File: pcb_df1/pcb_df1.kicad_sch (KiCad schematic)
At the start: 6 parts, among them J1 Cable, J2 Floppy, Q1 DMG2301L, Q2 BSS123

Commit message: DF1 (floppy detection) PCB completed.
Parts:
- J1, J2: footprint (none) -> pcb_df1:idc34_edge
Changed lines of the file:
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@@
       (effects (font (size 1.27 1.27)))
     )
-    (property "Footprint" "" (at 34.925 50.165 0)
+    (property "Footprint" "pcb_df1:idc34_edge" (at 34.925 50.165 0)
       (effects (font (size 1.27 1.27)) hide)
     )
@@
       (effects (font (size 1.27 1.27)))
     )
-    (property "Footprint" "" (at 72.39 50.165 0)
-      (effects (font (size 1.27 1.27)) hide)
-    )
+    (property "Footprint" "pcb_df1:idc34_edge" (at 72.39 50.165 0)
+      (effects (font (size 1.27 1.27)) hide)
+    )

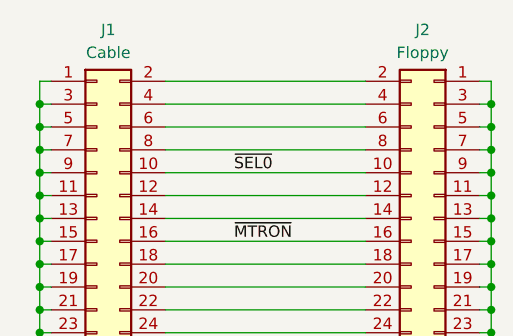
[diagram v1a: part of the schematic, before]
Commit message: DF1 board reworked
New version sits on the other end of the flat cable.
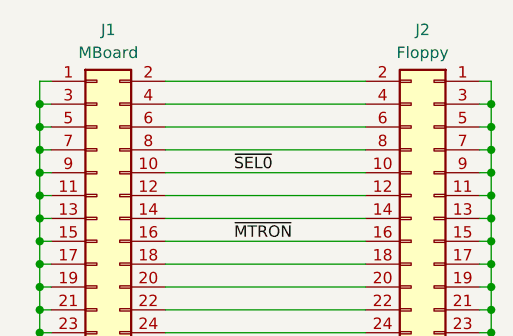
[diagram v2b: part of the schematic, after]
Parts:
- J1: value Cable -> MBoard; footprint pcb_df1:idc34_edge -> Connector_PinSocket_2.54mm:PinSocket_2x17_P2.54mm_Vertical
- J2: footprint pcb_df1:idc34_edge -> Connector_PinHeader_2.54mm:PinHeader_2x17_P2.54mm_Vertical
- R1, R2: footprint Resistor_SMD:R_0603_1608Metric_Pad0.98x0.95mm_HandSolder -> Resistor_SMD:R_0805_2012Metric_Pad1.20x1.40mm_HandSolder
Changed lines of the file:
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@@
       (effects (font (size 1.27 1.27)))
     )
-    (property "Value" "Cable" (at 36.195 26.67 0)
-      (effects (font (size 1.27 1.27)))
-    )
-    (property "Footprint" "pcb_df1:idc34_edge" (at 34.925 50.165 0)
+    (property "Value" "MBoard" (at 36.195 26.67 0)
+      (effects (font (size 1.27 1.27)))
+    )
+    (property "Footprint" "Connector_PinSocket_2.54mm:PinSocket_2x17_P2.54mm_Vertical" (at 34.925 50.165 0)
       (effects (font (size 1.27 1.27)) hide)
     )
@@
       (effects (font (size 1.27 1.27)))
     )
-    (property "Footprint" "Resistor_SMD:R_0603_1608Metric_Pad0.98x0.95mm_HandSolder" (at 163.83 48.133 90)
+    (property "Footprint" "Resistor_SMD:R_0805_2012Metric_Pad1.20x1.40mm_HandSolder" (at 163.83 48.133 90)
       (effects (font (size 1.27 1.27)) hide)
     )
@@
       (effects (font (size 1.27 1.27)) (justify left))
     )
-    (property "Footprint" "Resistor_SMD:R_0603_1608Metric_Pad0.98x0.95mm_HandSolder" (at 144.907 59.69 90)
+    (property "Footprint" "Resistor_SMD:R_0805_2012Metric_Pad1.20x1.40mm_HandSolder" (at 144.907 59.69 90)
       (effects (font (size 1.27 1.27)) hide)
     )
@@
       (effects (font (size 1.27 1.27)))
     )
-    (property "Footprint" "pcb_df1:idc34_edge" (at 72.39 50.165 0)
-      (effects (font (size 1.27 1.27)) hide)
-    )
+    (property "Footprint" "Connector_PinHeader_2.54mm:PinHeader_2x17_P2.54mm_Vertical" (at 72.39 50.165 0)
+      (effects (font (size 1.27 1.27)) hide)
+    )

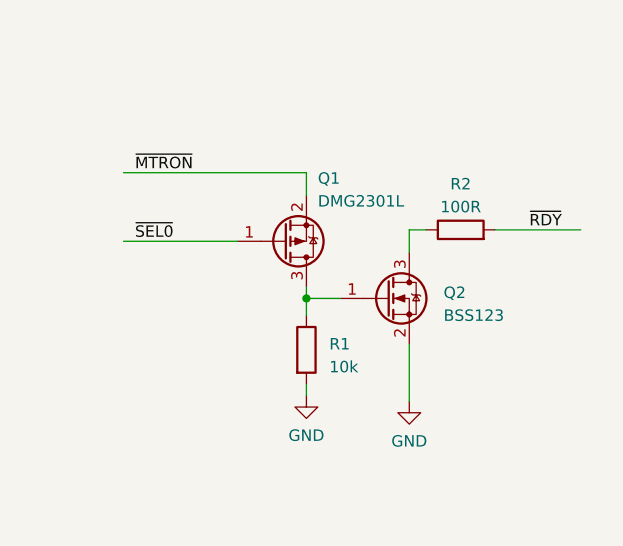
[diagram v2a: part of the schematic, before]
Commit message: DF1: R1 value fixed
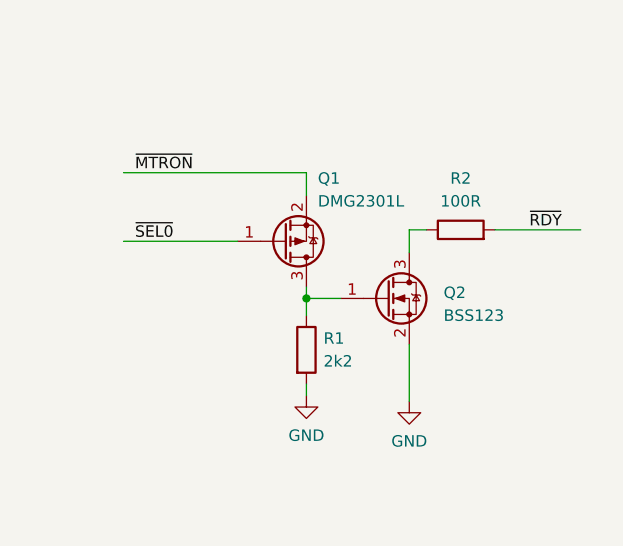
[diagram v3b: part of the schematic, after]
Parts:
- R1: value 10k -> 2k2
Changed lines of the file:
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@@
   (symbol (lib_id "Device:R") (at 163.83 46.355 90) (unit 1)
     (in_bom yes) (on_board yes) (dnp no) (fields_autoplaced)
-    (property "Reference" "R2" (at 163.83 41.275 90)
+    (property "Reference" "R2" (at 163.83 40.64 90)
       (effects (font (size 1.27 1.27)))
     )
-    (property "Value" "100R" (at 163.83 43.815 90)
+    (property "Value" "100R" (at 163.83 43.18 90)
       (effects (font (size 1.27 1.27)))
     )
@@
   (symbol (lib_id "Device:R") (at 146.685 59.69 0) (unit 1)
     (in_bom yes) (on_board yes) (dnp no) (fields_autoplaced)
-    (property "Reference" "R1" (at 149.225 59.055 0)
+    (property "Reference" "R1" (at 148.59 58.42 0)
       (effects (font (size 1.27 1.27)) (justify left))
     )
-    (property "Value" "10k" (at 149.225 61.595 0)
+    (property "Value" "2k2" (at 148.59 60.96 0)
       (effects (font (size 1.27 1.27)) (justify left))
     )
